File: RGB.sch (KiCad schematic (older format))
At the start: 10 parts, among them J9 LEDs, Q1 DMG2302UK, Q2 DMG2302UK, Q3 DMG2302UK

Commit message: Replaced the 10k-Resistor with one that is in stock
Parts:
- R28, R29, R30: Buy https://www.digikey.com/product-detail/en/yageo/RC0603FR-07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 -> https://www.digikey.com/product-detail/en/bourns-inc/CR0603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
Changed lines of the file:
@@
 F 2 "Resistor_SMD:R_0603_1608Metric" V 1630 2550 50  0001 C CNN
 F 3 "" H 1700 2550 50  0001 C CNN
-F 4 "https://www.digikey.com/product-detail/en/yageo/RC0603FR-0710KL/311-10.0KHRCT-ND/729827" V 1700 2550 50  0001 C CNN "Buy"
+F 4 "https://www.digikey.com/product-detail/en/bourns-inc/CR0603-FX-1002HLF/CR0603-FX-1002HLFCT-ND/3925297" V 1700 2550 50  0001 C CNN "Buy"
 	1    1700 2550
 	-1   0    0    1
@@
 F 2 "Resistor_SMD:R_0603_1608Metric" V 1455 2050 50  0001 C CNN
 F 3 "" H 1525 2050 50  0001 C CNN
-F 4 "https://www.digikey.com/product-detail/en/yageo/RC0603FR-0710KL/311-10.0KHRCT-ND/729827" V 1525 2050 50  0001 C CNN "Buy"
+F 4 "https://www.digikey.com/product-detail/en/bourns-inc/CR0603-FX-1002HLF/CR0603-FX-1002HLFCT-ND/3925297" V 1525 2050 50  0001 C CNN "Buy"
 	1    1525 2050
 	-1   0    0    1
@@
 F 2 "Resistor_SMD:R_0603_1608Metric" V 1280 1550 50  0001 C CNN
 F 3 "" H 1350 1550 50  0001 C CNN
-F 4 "https://www.digikey.com/product-detail/en/yageo/RC0603FR-0710KL/311-10.0KHRCT-ND/729827" V 1350 1550 50  0001 C CNN "Buy"
+F 4 "https://www.digikey.com/product-detail/en/bourns-inc/CR0603-FX-1002HLF/CR0603-FX-1002HLFCT-ND/3925297" V 1350 1550 50  0001 C CNN "Buy"
 	1    1350 1550
 	-1   0    0    1

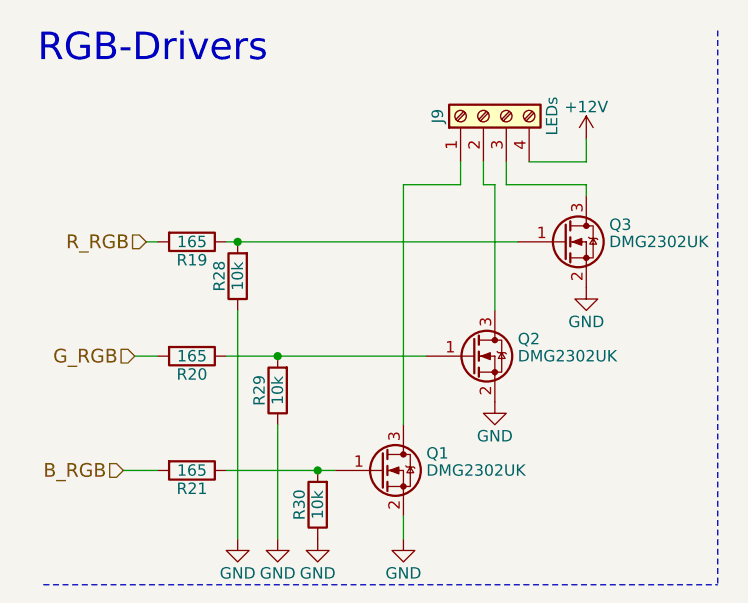
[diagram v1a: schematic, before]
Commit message: Filled in the Parts for the Fault-Indicator
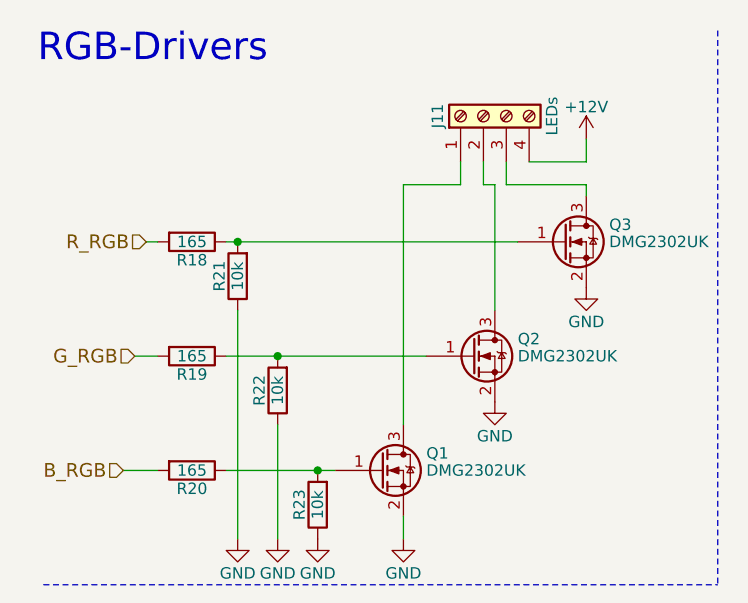
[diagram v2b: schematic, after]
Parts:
- renumbered J9 to J11, R19 to R18, R20 to R19, R21 to R20, R28 to R21, R29 to R22, R30 to R23
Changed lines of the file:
@@
 G_RGB
 $Comp
-L power:+12V #PWR078
+L power:+12V #PWR084
 U 1 1 5A83A3DF
 P 2875 950
-F 0 "#PWR078" H 2875 800 50  0001 C CNN
+F 0 "#PWR084" H 2875 800 50  0001 C CNN
 F 1 "+12V" H 2875 1090 50  0000 C CNN
 F 2 "" H 2875 950 50  0001 C CNN
@@
 	1300 1900 1525 1900
 $Comp
-L power:GND #PWR079
+L power:GND #PWR085
 U 1 1 5A83A3E9
 P 2875 1600
-F 0 "#PWR079" H 2875 1350 50  0001 C CNN
+F 0 "#PWR085" H 2875 1350 50  0001 C CNN
 F 1 "GND" H 2875 1450 50  0000 C CNN
 F 2 "" H 2875 1600 50  0001 C CNN
@@
 $EndComp
 $Comp
-L power:GND #PWR077
+L power:GND #PWR083
 U 1 1 5A83A3EF
 P 2475 2100
-F 0 "#PWR077" H 2475 1850 50  0001 C CNN
+F 0 "#PWR083" H 2475 1850 50  0001 C CNN
 F 1 "GND" H 2475 1950 50  0000 C CNN
 F 2 "" H 2475 2100 50  0001 C CNN
@@
 $EndComp
 $Comp
-L power:GND #PWR076
+L power:GND #PWR082
 U 1 1 5A83A3F5
 P 2075 2700
-F 0 "#PWR076" H 2075 2450 50  0001 C CNN
+F 0 "#PWR082" H 2075 2450 50  0001 C CNN
 F 1 "GND" H 2075 2550 50  0000 C CNN
 F 2 "" H 2075 2700 50  0001 C CNN
@@
 	1300 2400 1700 2400
 $Comp
-L Device:R R19
+L Device:R R18
 U 1 1 5A8936F2
 P 1150 1400
-F 0 "R19" V 1230 1400 50  0000 C CNN
+F 0 "R18" V 1230 1400 50  0000 C CNN
 F 1 "165" V 1150 1400 50  0000 C CNN
 F 2 "Resistor_SMD:R_0603_1608Metric" V 1080 1400 50  0001 C CNN
@@
 	1300 1400 1350 1400
 $Comp
-L Device:R R20
+L Device:R R19
 U 1 1 5A8938B9
 P 1150 1900
-F 0 "R20" V 1230 1900 50  0000 C CNN
+F 0 "R19" V 1230 1900 50  0000 C CNN
 F 1 "165" V 1150 1900 50  0000 C CNN
 F 2 "Resistor_SMD:R_0603_1608Metric" V 1080 1900 50  0001 C CNN
@@
 	1000 1900 900  1900
 $Comp
-L Device:R R21
+L Device:R R20
 U 1 1 5A8939A3
 P 1150 2400
-F 0 "R21" V 1230 2400 50  0000 C CNN
+F 0 "R20" V 1230 2400 50  0000 C CNN
 F 1 "165" V 1150 2400 50  0000 C CNN
 F 2 "Resistor_SMD:R_0603_1608Metric" V 1080 2400 50  0001 C CNN
@@
 	1000 2400 850  2400
 $Comp
-L Connector_Specialized:Screw_Terminal_01x04 J9
+L Connector_Specialized:Screw_Terminal_01x04 J11
 U 1 1 5A84BDDF
 P 2425 850
-F 0 "J9" H 2425 1050 50  0000 C CNN
+F 0 "J11" H 2425 1050 50  0000 C CNN
 F 1 "LEDs" H 2425 550 50  0000 C CNN
 F 2 "TerminalBlock:TerminalBlock_bornier-4_P5.08mm" H 2425 850 50  0001 C CNN
@@
 	2875 1050 2625 1050
 $Comp
-L Device:R R30
+L Device:R R23
 U 1 1 5AB7367D
 P 1700 2550
-F 0 "R30" V 1780 2550 50  0000 C CNN
+F 0 "R23" V 1780 2550 50  0000 C CNN
 F 1 "10k" V 1700 2550 50  0000 C CNN
 F 2 "Resistor_SMD:R_0603_1608Metric" V 1630 2550 50  0001 C CNN
@@
 Connection ~ 1700 2400
 $Comp
-L Device:R R29
+L Device:R R22
 U 1 1 5AB73ADE
 P 1525 2050
-F 0 "R29" V 1605 2050 50  0000 C CNN
+F 0 "R22" V 1605 2050 50  0000 C CNN
 F 1 "10k" V 1525 2050 50  0000 C CNN
 F 2 "Resistor_SMD:R_0603_1608Metric" V 1455 2050 50  0001 C CNN
@@
 	1525 1900 2175 1900
 $Comp
-L Device:R R28
+L Device:R R21
 U 1 1 5AB73B36
 P 1350 1550
-F 0 "R28" V 1430 1550 50  0000 C CNN
+F 0 "R21" V 1430 1550 50  0000 C CNN
 F 1 "10k" V 1350 1550 50  0000 C CNN
 F 2 "Resistor_SMD:R_0603_1608Metric" V 1280 1550 50  0001 C CNN
@@
 	1350 1400 2575 1400
 $Comp
-L power:GND #PWR0102
+L power:GND #PWR081
 U 1 1 5AB73BDF
 P 1700 2700
-F 0 "#PWR0102" H 1700 2450 50  0001 C CNN
+F 0 "#PWR081" H 1700 2450 50  0001 C CNN
 F 1 "GND" H 1700 2550 50  0000 C CNN
 F 2 "" H 1700 2700 50  0001 C CNN
@@
 $EndComp
 $Comp
-L power:GND #PWR0103
+L power:GND #PWR080
 U 1 1 5AB73BFE
 P 1525 2700
-F 0 "#PWR0103" H 1525 2450 50  0001 C CNN
+F 0 "#PWR080" H 1525 2450 50  0001 C CNN
 F 1 "GND" H 1525 2550 50  0000 C CNN
 F 2 "" H 1525 2700 50  0001 C CNN
@@
 $EndComp
 $Comp
-L power:GND #PWR0104
+L power:GND #PWR079
 U 1 1 5AB73C1D
 P 1350 2700
-F 0 "#PWR0104" H 1350 2450 50  0001 C CNN
+F 0 "#PWR079" H 1350 2450 50  0001 C CNN
 F 1 "GND" H 1350 2550 50  0000 C CNN
 F 2 "" H 1350 2700 50  0001 C CNN

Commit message: Migrated connectors to new libraries
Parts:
- J11: symbol Connector_Specialized:Screw_Terminal_01x04 -> Connector:Screw_Terminal_01x04
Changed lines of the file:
@@
 	1000 2400 850  2400
 $Comp
-L Connector_Specialized:Screw_Terminal_01x04 J11
+L Connector:Screw_Terminal_01x04 J11
 U 1 1 5A84BDDF
 P 2425 850

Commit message: Replaced OOS 10k-Resistor
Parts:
- R21, R22, R23: Buy https://www.digikey.com/product-detail/en/bourns-inc/CR0603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 -> https://www.digikey.com/short/jw22d4
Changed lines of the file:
@@
 F 2 "Resistor_SMD:R_0603_1608Metric" V 1630 2550 50  0001 C CNN
 F 3 "" H 1700 2550 50  0001 C CNN
-F 4 "https://www.digikey.com/product-detail/en/bourns-inc/CR0603-FX-1002HLF/CR0603-FX-1002HLFCT-ND/3925297" V 1700 2550 50  0001 C CNN "Buy"
+F 4 "https://www.digikey.com/short/jw22d4" V 1700 2550 50  0001 C CNN "Buy"
 	1    1700 2550
 	-1   0    0    1
@@
 F 2 "Resistor_SMD:R_0603_1608Metric" V 1455 2050 50  0001 C CNN
 F 3 "" H 1525 2050 50  0001 C CNN
-F 4 "https://www.digikey.com/product-detail/en/bourns-inc/CR0603-FX-1002HLF/CR0603-FX-1002HLFCT-ND/3925297" V 1525 2050 50  0001 C CNN "Buy"
+F 4 "https://www.digikey.com/short/jw22d4" V 1525 2050 50  0001 C CNN "Buy"
 	1    1525 2050
 	-1   0    0    1
@@
 F 2 "Resistor_SMD:R_0603_1608Metric" V 1280 1550 50  0001 C CNN
 F 3 "" H 1350 1550 50  0001 C CNN
-F 4 "https://www.digikey.com/product-detail/en/bourns-inc/CR0603-FX-1002HLF/CR0603-FX-1002HLFCT-ND/3925297" V 1350 1550 50  0001 C CNN "Buy"
+F 4 "https://www.digikey.com/short/jw22d4" V 1350 1550 50  0001 C CNN "Buy"
 	1    1350 1550
 	-1   0    0    1

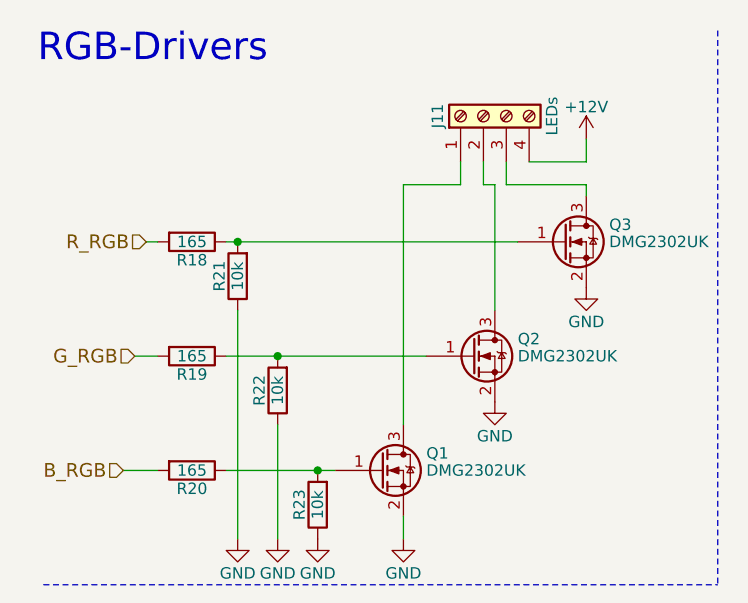
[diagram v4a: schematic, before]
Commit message: Added TestPoints the RGB-Schematic
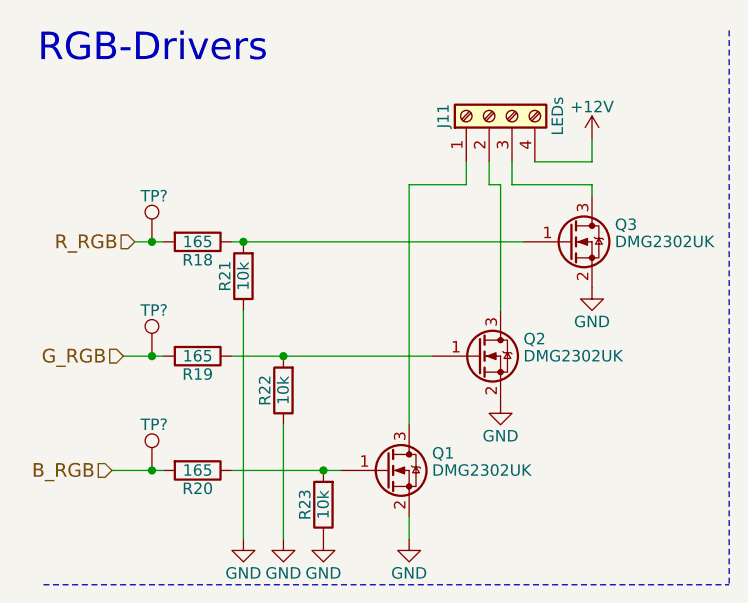
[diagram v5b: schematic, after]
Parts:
- added TP? (x3): TestPoint, symbol Connector:TestPoint
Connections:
- net B_RGB: now also TP?.1
- net G_RGB: now also TP?.1
- net R_RGB: now also TP?.1
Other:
- moved on the sheet: J11, Q1, Q2, Q3, R18, R19, R20, R21, R22, R23
